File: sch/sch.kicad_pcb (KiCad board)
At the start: 2 copper layers, 53 parts, among them U1 Pico, U2 PCA9548ADB, U3 MPR121QR2_BOARD, U4 MPR121QR2_BOARD, U5 MPR121QR2_BOARD

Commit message: Updated schematic for Pro Micro
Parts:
- removed U1: Pico, MCU_RaspberryPi_and_Boards:RPi_Pico_SMD_TH
- added REF**: MountingHole_3.2mm_M3_DIN965_Pad, MountingHole:MountingHole_3.2mm_M3_DIN965_Pad, F.Cu at (269.1, 139.2)
- added REF**: MountingHole_3.2mm_M3_DIN965_Pad, MountingHole:MountingHole_3.2mm_M3_DIN965_Pad, F.Cu at (25.0, 45.0)
- added REF**: MountingHole_3.2mm_M3_DIN965_Pad, MountingHole:MountingHole_3.2mm_M3_DIN965_Pad, F.Cu at (269.1, 44.5)
- added REF**: MountingHole_3.2mm_M3_DIN965_Pad, MountingHole:MountingHole_3.2mm_M3_DIN965_Pad, F.Cu at (24.9, 139.2)
- added U6: ProMicro, promicro:ProMicro, F.Cu at (73.2, 58.4)
- moved KEY31 33.6 mm to (154.9, 89.2)
- moved KEY30 27.4 mm to (169.5, 116.0)
- moved R3 14.9 mm to (130.3, 133.1), turned to 180 degrees
- moved R4 14.6 mm to (130.3, 136.6), turned to 180 degrees
- moved KEY11 13.7 mm to (131.3, 48.8), turned to -90 degrees
- moved KEY9 13.1 mm to (191.6, 48.8), turned to -90 degrees
- moved TOF4 12.2 mm to (234.5, 139.6)
- moved TOF2 10.3 mm to (102.4, 139.6)
- moved R8 10.1 mm to (218.7, 133.1)
- moved R6 10.1 mm to (167.3, 132.9)
- moved R1 10.1 mm to (83.7, 133.4), turned to 180 degrees
- moved R2 10.0 mm to (83.7, 136.6), turned to 180 degrees
- moved U3 7.81 mm to (101.2, 68.5)
- moved U5 7.57 mm to (223.1, 68.5)
- moved KEY10 7.50 mm to (191.6, 63.4), turned to -90 degrees
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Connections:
- U2 pad 3: /MX_RST -> (no net)
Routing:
- net +3.3V: track 0.00 -> 517.3 mm, vias 0 -> 1
- net GND: track 0.00 -> 506.5 mm, vias 0 -> 1
- net /SDA: track 0.00 -> 387.2 mm, vias 0 -> 1
- net /SCL: track 0.00 -> 381.9 mm, vias 0 -> 1
- net /SDA4: track 0.00 -> 114.3 mm, vias 0 -> 2
- net /SCL4: track 0.00 -> 111.0 mm, vias 0 -> 2
- net /SCL1: track 0.00 -> 106.3 mm, vias 0 -> 4
- net /SDA1: track 0.00 -> 93.0 mm, vias 0 -> 2
- net Net-(KEY24-Pin_1): track 0.00 -> 91.6 mm, vias 0 -> 1
- net Net-(KEY11-Pin_1): track 0.00 -> 88.1 mm, vias 0 -> 1
- net Net-(KEY22-Pin_1): track 0.00 -> 83.4 mm, vias 0 -> 1
- net Net-(KEY12-Pin_1): track 0.00 -> 79.5 mm, vias 0 -> 1
- net Net-(KEY20-Pin_1): track 0.00 -> 73.6 mm, vias 0 -> 1
- net Net-(KEY26-Pin_1): track 0.00 -> 69.4 mm, vias 0 -> 1
- net Net-(KEY23-Pin_1): track 0.00 -> 68.3 mm
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- added copper zone on B.Cu, net GND
- added copper zone on F.Cu, net GND
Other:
- board outline added: 254.1 x 104.6 mm

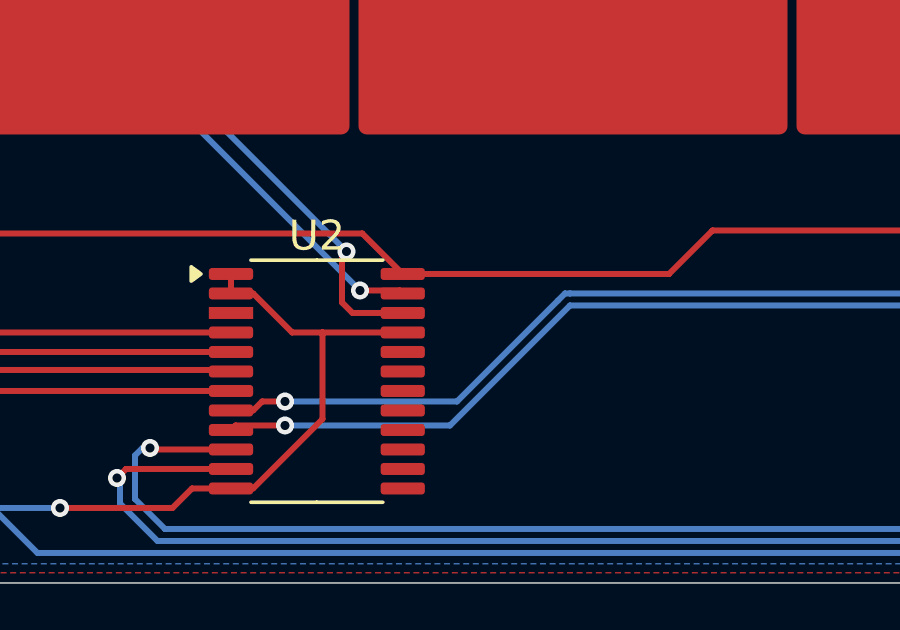
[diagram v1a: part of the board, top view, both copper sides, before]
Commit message: fixed missing pull up on multiplexer
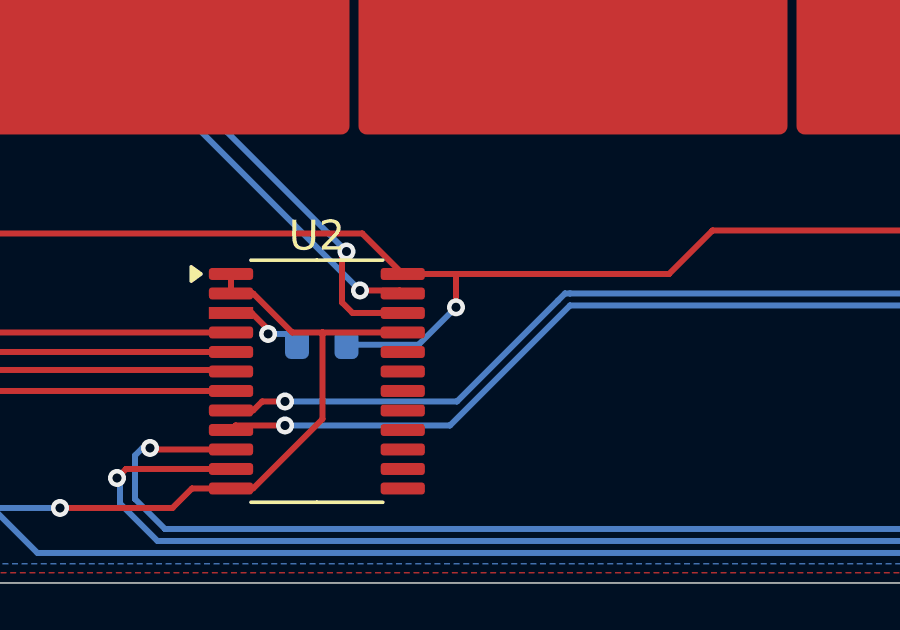
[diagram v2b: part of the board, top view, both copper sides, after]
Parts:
- added R9: 4.7K, Resistor_SMD:R_0603_1608Metric, B.Cu at (146.5, 136.7)
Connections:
- U2 pad 3: (no net) -> Net-(U2-~{RESET})
- U6 pad 18: (no net) -> unconnected-(U6-F6-Pad18)
- U6 pad 22: unconnected-(U6-RST-Pad22) -> GND
- U6 pad 23: GND -> unconnected-(U6-GND-Pad23)
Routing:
- net +3.3V: track 517.3 -> 522.5 mm, vias 1 -> 2
- net Net-(U2-~{RESET}): track 0.00 -> 2.74 mm, vias 0 -> 1

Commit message: Revision 2 of the PCB
Updated to using stm32f4 and a more modular design
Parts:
- removed KEY10, KEY11, KEY12, KEY13, KEY14, KEY15, KEY16, KEY17, KEY18, KEY19, KEY20, KEY21, KEY22, KEY23, KEY24, KEY25, KEY26, KEY27, KEY28, KEY29, KEY30, KEY31, KEY32, KEY33, KEY34, KEY35, KEY36, KEY9: Conn_01x01, chu_main:ChuKey
- removed REF** (x4): MountingHole_3.2mm_M3_DIN965_Pad, MountingHole:MountingHole_3.2mm_M3_DIN965_Pad
- removed TOF1, TOF2, TOF3, TOF4: Conn_01x06, Connector_PinSocket_2.54mm:PinSocket_1x06_P2.54mm_Vertical
- added C1: 10u, Capacitor_SMD:C_0603_1608Metric_Pad1.08x0.95mm_HandSolder, F.Cu at (157.6, 41.1)
- added C10: 100n, Capacitor_SMD:C_0603_1608Metric_Pad1.08x0.95mm_HandSolder, F.Cu at (170.5, 47.0)
- added C11: 100n, Capacitor_SMD:C_0603_1608Metric_Pad1.08x0.95mm_HandSolder, F.Cu at (158.3, 66.4)
- added C12: 33p, Capacitor_SMD:C_0603_1608Metric_Pad1.08x0.95mm_HandSolder, F.Cu at (171.0, 54.0)
- added C13: 33p, Capacitor_SMD:C_0603_1608Metric_Pad1.08x0.95mm_HandSolder, F.Cu at (171.0, 50.5)
- added C14: 22u, Capacitor_SMD:C_0805_2012Metric, F.Cu at (128.4, 50.5)
- added C15: 22u, Capacitor_SMD:C_0805_2012Metric, F.Cu at (133.4, 56.0)
- added C16: 100n, Capacitor_SMD:C_0603_1608Metric_Pad1.08x0.95mm_HandSolder, F.Cu at (131.6, 77.5)
- added C17: 100n, Capacitor_SMD:C_0603_1608Metric_Pad1.08x0.95mm_HandSolder, F.Cu at (144.1, 77.5)
- added C18: 100n, Capacitor_SMD:C_0603_1608Metric_Pad1.08x0.95mm_HandSolder, F.Cu at (160.5, 77.7)
- added C19: 100n, Capacitor_SMD:C_0603_1608Metric_Pad1.08x0.95mm_HandSolder, F.Cu at (172.9, 77.8)
- added C2: 100n, Capacitor_SMD:C_0603_1608Metric_Pad1.08x0.95mm_HandSolder, F.Cu at (168.1, 55.4)
- added C3: 100n, Capacitor_SMD:C_0603_1608Metric_Pad1.08x0.95mm_HandSolder, F.Cu at (164.3, 42.7)
- added C4: 100n, Capacitor_SMD:C_0603_1608Metric_Pad1.08x0.95mm_HandSolder, F.Cu at (157.6, 42.7)
- added C5: 100n, Capacitor_SMD:C_0603_1608Metric_Pad1.08x0.95mm_HandSolder, F.Cu at (152.9, 54.9)
- added C6: 100n, Capacitor_SMD:C_0603_1608Metric_Pad1.08x0.95mm_HandSolder, F.Cu at (165.1, 58.1)
- added C7: 10n, Capacitor_SMD:C_0603_1608Metric_Pad1.08x0.95mm_HandSolder, F.Cu at (168.2, 48.9)
- added C8: 1u, Capacitor_SMD:C_0603_1608Metric_Pad1.08x0.95mm_HandSolder, F.Cu at (171.1, 43.0)
- added C9: 1u, Capacitor_SMD:C_0603_1608Metric_Pad1.08x0.95mm_HandSolder, F.Cu at (171.1, 41.4)
- added D1: RED, LED_SMD:LED_0201_0603Metric, F.Cu at (123.2, 55.8)
- added D2: WS2812B, LED_SMD:LED_WS2812B_PLCC4_5.0x5.0mm_P3.2mm, F.Cu at (131.6, 81.2)
- added D3: WS2812B, LED_SMD:LED_WS2812B_PLCC4_5.0x5.0mm_P3.2mm, F.Cu at (144.0, 81.2)
- added D4: WS2812B, LED_SMD:LED_WS2812B_PLCC4_5.0x5.0mm_P3.2mm, F.Cu at (160.5, 81.3)
- added D5: WS2812B, LED_SMD:LED_WS2812B_PLCC4_5.0x5.0mm_P3.2mm, F.Cu at (172.9, 81.4)
- added FB1: 120R, Inductor_SMD:L_0603_1608Metric, F.Cu at (168.4, 42.2)
- added J1: USB_C_Receptacle_USB2.0_16P, Connector_USB:USB_C_Receptacle_GCT_USB4105-xx-A_16P_TopMnt_Horizontal, F.Cu at (134.5, 43.1)
- added J2: Conn_01x04_Pin, Connector_PinHeader_2.54mm:PinHeader_1x04_P2.54mm_Vertical, F.Cu at (150.2, 41.5)
- added J3: Conn_01x04, chu_main:Conn_Solder_I2C, F.Cu at (181.4, 72.5)
- added J4: Conn_01x06_Socket, Connector_PinHeader_2.54mm:PinHeader_1x06_P2.54mm_Vertical, F.Cu at (146.2, 146.0)
- added J5: Conn_01x04, chu_main:Conn_Solder_I2C, F.Cu at (123.0, 72.5)
- added J6: Conn_01x01, chu_main:Solder_3P, F.Cu at (121.9, 80.5)
- added J7: Conn_01x01, chu_main:Solder_3P, F.Cu at (182.5, 80.5)
- added MH1: M3, MountingHole:MountingHole_3.2mm_M3_Pad_Via, F.Cu at (122.5, 43.5)
- added MH2: M3, MountingHole:MountingHole_3.2mm_M3_Pad_Via, F.Cu at (181.5, 43.5)
- added MH3: M3, MountingHole:MountingHole_3.2mm_M3_Pad_Via, F.Cu at (122.5, 145.5)
- added MH4: M3, MountingHole:MountingHole_3.2mm_M3_Pad_Via, F.Cu at (181.5, 145.5)
- added R10: 2k2, Resistor_SMD:R_0603_1608Metric_Pad0.98x0.95mm_HandSolder, F.Cu at (140.0, 56.0)
- added R11: 0, Resistor_SMD:R_0603_1608Metric_Pad0.98x0.95mm_HandSolder, F.Cu at (144.0, 68.2)
- added R12: 0, Resistor_SMD:R_0603_1608Metric_Pad0.98x0.95mm_HandSolder, F.Cu at (147.0, 68.2)
- added R13: 2k2, Resistor_SMD:R_0603_1608Metric_Pad0.98x0.95mm_HandSolder, F.Cu at (163.2, 59.9)
- added R14: 2k2, Resistor_SMD:R_0603_1608Metric_Pad0.98x0.95mm_HandSolder, F.Cu at (159.9, 59.9)
- added R15: 0, Resistor_SMD:R_0603_1608Metric_Pad0.98x0.95mm_HandSolder, F.Cu at (150.0, 68.2)
- added R16: 2k2, Resistor_SMD:R_0603_1608Metric_Pad0.98x0.95mm_HandSolder, F.Cu at (140.6, 65.3)
- added R17: 0, Resistor_SMD:R_0603_1608Metric_Pad0.98x0.95mm_HandSolder, F.Cu at (153.0, 68.2)
- added R18: 0, Resistor_SMD:R_0603_1608Metric_Pad0.98x0.95mm_HandSolder, F.Cu at (142.5, 68.2)
- added R19: 0, Resistor_SMD:R_0603_1608Metric_Pad0.98x0.95mm_HandSolder, F.Cu at (145.5, 68.2)
- added R20: 0, Resistor_SMD:R_0603_1608Metric_Pad0.98x0.95mm_HandSolder, F.Cu at (148.5, 68.2)
- added R21: 0, Resistor_SMD:R_0603_1608Metric_Pad0.98x0.95mm_HandSolder, F.Cu at (151.5, 68.2)
- added R22: 2k2, Resistor_SMD:R_0603_1608Metric_Pad0.98x0.95mm_HandSolder, F.Cu at (140.8, 145.2)
- added R23: 2k2, Resistor_SMD:R_0603_1608Metric_Pad0.98x0.95mm_HandSolder, F.Cu at (140.8, 146.8)
- added R24: 1k, Resistor_SMD:R_0603_1608Metric_Pad0.98x0.95mm_HandSolder, F.Cu at (123.2, 58.7)
- added RST: SW_SPST, Button_Switch_SMD:SW_SPST_TS-1088-xR025, F.Cu at (172.0, 61.1)
- added U1: MPR121QR2, Package_DFN_QFN:UQFN-20_3x3mm_P0.4mm, F.Cu at (162.0, 68.5)
- added Y1: 25MHz, Crystal:Crystal_SMD_3225-4Pin_3.2x2.5mm_HandSoldering, F.Cu at (174.2, 52.1)
- R1, R2, R3, R4: value 4.7K -> 0; footprint Resistor_SMD:R_0603_1608Metric -> Resistor_SMD:R_0603_1608Metric_Pad0.98x0.95mm_HandSolder
- R5: value 4.7K -> 10K; footprint Resistor_SMD:R_0603_1608Metric -> Resistor_SMD:R_0603_1608Metric_Pad0.98x0.95mm_HandSolder
- R6, R8: value 4.7K -> 5.1K; footprint Resistor_SMD:R_0603_1608Metric -> Resistor_SMD:R_0603_1608Metric_Pad0.98x0.95mm_HandSolder
- R7: value 4.7K -> 75K; footprint Resistor_SMD:R_0603_1608Metric -> Resistor_SMD:R_0603_1608Metric_Pad0.98x0.95mm_HandSolder
- R9: value 4.7K -> 2k2; footprint Resistor_SMD:R_0603_1608Metric -> Resistor_SMD:R_0603_1608Metric_Pad0.98x0.95mm_HandSolder; moved to F.Cu
- U2: value PCA9548ADB -> STM32F411R_C-E_Tx; footprint Package_SO:TSSOP-24_4.4x7.8mm_P0.65mm -> Package_QFP:LQFP-64_10x10mm_P0.5mm
- U3: value MPR121QR2_BOARD -> PCA9548ADB; footprint chu_main:MPR121_BOARD -> Package_SO:TSSOP-24_4.4x7.8mm_P0.65mm; moved to F.Cu
- U4: value MPR121QR2_BOARD -> AMS1117-3.3; footprint chu_main:MPR121_BOARD -> Package_TO_SOT_SMD:SOT-223-3_TabPin2; moved to F.Cu
- U5: value MPR121QR2_BOARD -> SN74LV1T34DBV; footprint chu_main:MPR121_BOARD -> Package_TO_SOT_SMD:SOT-23-5; moved to F.Cu
- U6: value ProMicro -> USBLC6-2SC6; footprint promicro:ProMicro -> Package_TO_SOT_SMD:SOT-23-6
- moved KEY2 129.9 mm to (127.7, 126.1), turned to 0 degrees
- moved KEY1 129.8 mm to (127.7, 98.1), turned to 0 degrees
- moved R8 125.7 mm to (128.0, 46.1), turned to 90 degrees
- moved R2 103.9 mm to (157.6, 63.6), turned to 90 degrees
- moved R1 100.6 mm to (156.1, 63.6), turned to 90 degrees
- moved KEY4 99.1 mm to (144.0, 126.1), turned to 0 degrees
- moved KEY3 99.0 mm to (144.0, 98.0), turned to 0 degrees
- moved R7 91.4 mm to (157.4, 68.9), turned to 90 degrees
- moved R6 90.7 mm to (141.0, 46.1), turned to 90 degrees
- moved U2 88.7 mm to (160.5, 50.3), turned to 180 degrees
- moved U5 87.5 mm to (135.8, 62.2), turned to 90 degrees
- moved R9 81.1 mm to (138.5, 56.0), turned to 90 degrees
- moved R4 79.5 mm to (160.1, 62.9), turned to 0 degrees
- moved R3 74.8 mm to (160.0, 64.5), turned to 0 degrees
- moved U6 73.9 mm to (146.9, 52.3), turned to 0 degrees
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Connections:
- R1 pad 1: +3.3V -> /MPR121_ADDR
- R1 pad 2: /SCL1 -> GND
- R2 pad 1: +3.3V -> /MPR121_ADDR
- R2 pad 2: /SDA1 -> +3.3V
- R3 pad 1: +3.3V -> /MPR121_ADDR
- R3 pad 2: /SCL2 -> /I2C1_SDA
- R4 pad 1: +3.3V -> /MPR121_ADDR
- R4 pad 2: /SDA2 -> /I2C1_SCL
- R5 pad 1: +3.3V -> Net-(SW1-A)
- R5 pad 2: /SCL3 -> /BOOT0
- R6 pad 1: +3.3V -> GND
- R6 pad 2: /SDA3 -> /USB_CC1
- R7 pad 1: +3.3V -> Net-(U1-REXT)
- R7 pad 2: /SCL4 -> GND
- R8 pad 1: +3.3V -> GND
- R8 pad 2: /SDA4 -> /USB_CC2
- R9 pad 2: Net-(U2-~{RESET}) -> /I2C3_SDA
- U2 pad 1: GND -> +3.3V
- U2 pad 10: /SDA4 -> unconnected-(U2-PC2-Pad10)
- U2 pad 11: /SCL4 -> unconnected-(U2-PC3-Pad11)
- U2 pad 13: unconnected-(U2-SD4-Pad13) -> +3.3VA
- U2 pad 18: unconnected-(U2-SC6-Pad18) -> GND
- U2 pad 19: unconnected-(U2-SD7-Pad19) -> +3.3V
- U2 pad 2: GND -> unconnected-(U2-PC13-Pad2)
- U2 pad 21: GND -> unconnected-(U2-PA5-Pad21)
- U2 pad 22: /SCL -> unconnected-(U2-PA6-Pad22)
- U2 pad 23: /SDA -> unconnected-(U2-PA7-Pad23)
- U2 pad 24: +3.3V -> unconnected-(U2-PC4-Pad24)
- U2 pad 3: Net-(U2-~{RESET}) -> unconnected-(U2-PC14-Pad3)
- U2 pad 4: /SDA1 -> unconnected-(U2-PC15-Pad4)
- U2 pad 5: /SCL1 -> /HSE_IN
- U2 pad 6: /SDA2 -> /HSE_OUT
- U2 pad 7: /SCL2 -> /NRST
- U2 pad 8: /SDA3 -> unconnected-(U2-PC0-Pad8)
- U2 pad 9: /SCL3 -> unconnected-(U2-PC1-Pad9)
- U3 pad 1: unconnected-(U3-~{IRQ}-Pad1) -> GND
- U3 pad 10: Net-(KEY15-Pin_1) -> /SDA4
- U3 pad 11: Net-(KEY16-Pin_1) -> /SCL4
- U3 pad 12: Net-(KEY17-Pin_1) -> GND
- U3 pad 13: Net-(KEY18-Pin_1) -> unconnected-(U3-SD4-Pad13)
- U3 pad 14: Net-(KEY19-Pin_1) -> unconnected-(U3-SC4-Pad14)
- U3 pad 15: Net-(KEY20-Pin_1) -> unconnected-(U3-SD5-Pad15)
- U3 pad 16: Net-(KEY21-Pin_1) -> unconnected-(U3-SC5-Pad16)
- U3 pad 17: Net-(KEY22-Pin_1) -> unconnected-(U3-SD6-Pad17)
- U3 pad 18: Net-(KEY23-Pin_1) -> unconnected-(U3-SC6-Pad18)
- U3 pad 19: Net-(KEY24-Pin_1) -> unconnected-(U3-SD7-Pad19)
- U3 pad 2: /SCL -> GND
- U3 pad 20: +3.3V -> unconnected-(U3-SC7-Pad20)
- U3 pad 3: /SDA -> Net-(U3-~{RESET})
- U3 pad 4: +3.3V -> /SDA1
- U3 pad 6: GND -> /SDA2
- U3 pad 8: Net-(KEY13-Pin_1) -> /SDA3
- U3 pad 9: Net-(KEY14-Pin_1) -> /SCL3
- U4 pad 1: unconnected-(U4-~{IRQ}-Pad1) -> GND
- U4 pad 2: /SCL -> +3.3V
- U4 pad 3: /SDA -> VBUS
- U5 pad 2: /SCL -> Net-(D2-DIN)
- U5 pad 3: /SDA -> GND
- U5 pad 4: GND -> /LED_DIN
- U6 pad 1: unconnected-(U6-TX-Pad1) -> /USB_D-
- U6 pad 2: unconnected-(U6-RX-Pad2) -> GND
- U6 pad 3: GND -> /USB_D+
- U6 pad 4: GND -> /USB_D+
- U6 pad 5: /SDA -> VBUS
- U6 pad 6: /SCL -> /USB_D-
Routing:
- net GND: track 506.5 -> 14.8 mm, vias 1 -> 54
- net /SDA: track 387.2 -> 0.00 mm, vias 1 -> 0
- net /SCL: track 381.9 -> 0.00 mm, vias 1 -> 0
- net +3.3V: track 522.5 -> 280.2 mm, vias 2 -> 14
- net /SDA_ToF: track 0.00 -> 187.6 mm, vias 0 -> 2
- net /SCL_ToF: track 0.00 -> 184.7 mm, vias 0 -> 2
- net VBUS: track 0.00 -> 125.2 mm, vias 0 -> 6
- net /SDA4: track 114.3 -> 4.63 mm, vias 2 -> 0
- net /SCL4: track 111.0 -> 5.57 mm, vias 2 -> 0
- net /SCL1: track 106.3 -> 4.74 mm, vias 4 -> 0
- net Net-(KEY24-Pin_1): track 91.6 -> 0.00 mm, vias 1 -> 0
- net Net-(KEY11-Pin_1): track 88.1 -> 0.00 mm, vias 1 -> 0
- net /SDA1: track 93.0 -> 5.53 mm, vias 2 -> 0
- net /I2C1_SCL: track 0.00 -> 84.5 mm, vias 0 -> 4
- net Net-(KEY22-Pin_1): track 83.4 -> 0.00 mm, vias 1 -> 0
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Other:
- board size 254.1 x 104.6 mm -> 67 x 110 mm
- rule pad_to_mask_clearance: 0 -> 0.1

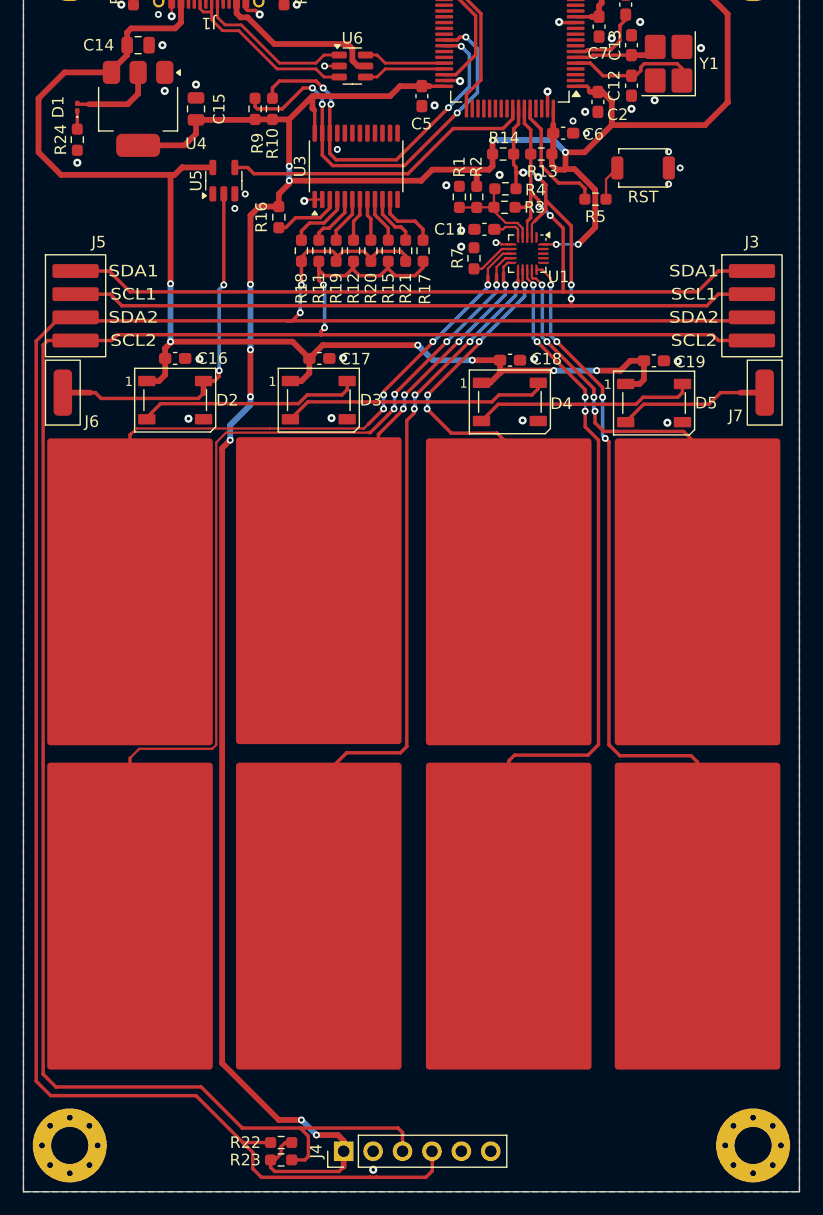
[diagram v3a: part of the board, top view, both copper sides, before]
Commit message: Updated side pads with power and ground
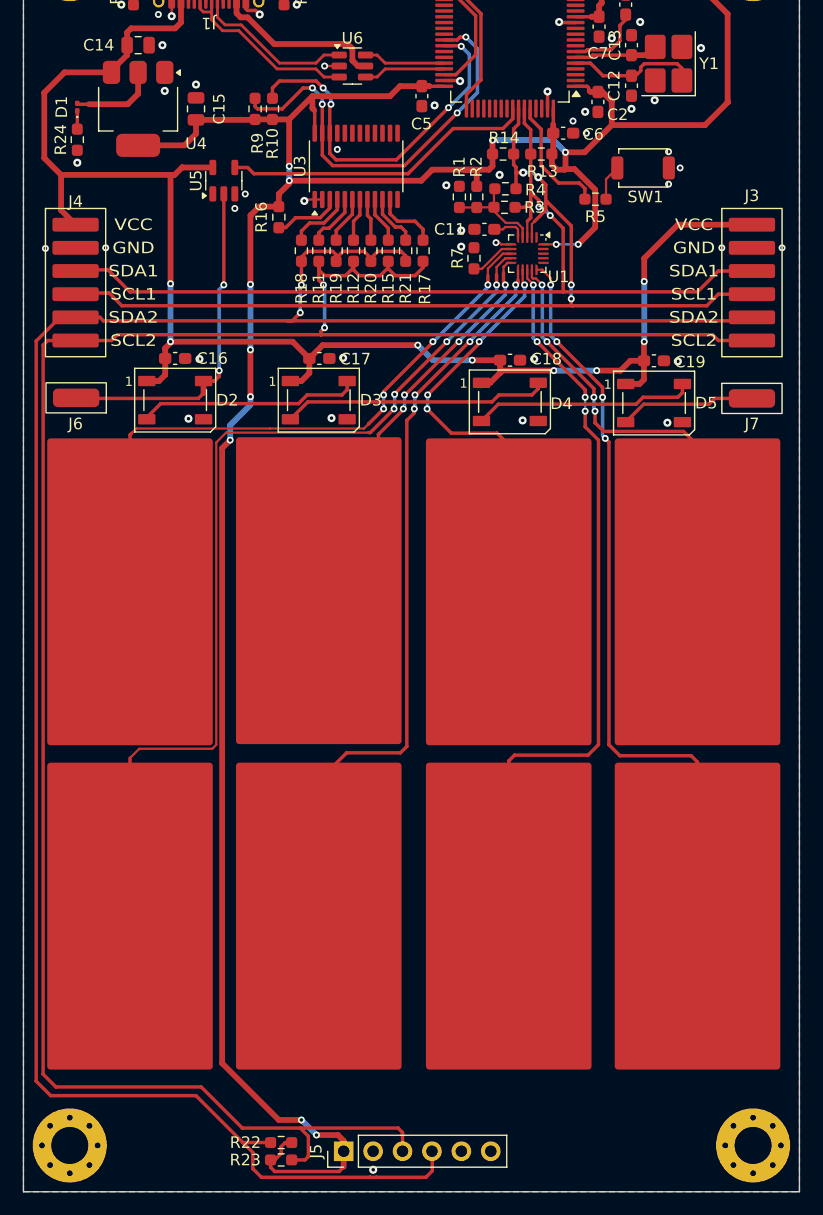
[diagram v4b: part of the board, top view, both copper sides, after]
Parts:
- J3: value Conn_01x04 -> Conn_01x06
- J4: renamed from J5; value Conn_01x04 -> Conn_01x06
- moved J4 1.50 mm to (123.0, 71.0)
- moved J6 1.23 mm to (123.0, 81.0), turned to 180 degrees
- moved J7 1.21 mm to (181.4, 81.0), turned to 0 degrees
- renumbered J4 to J5, RST to SW1
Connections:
- J3 pad 1: /I2C1_SDA -> VBUS
- J3 pad 2: /I2C1_SCL -> GND
- J3 pad 3: /SDA_ToF -> /I2C1_SDA
- J3 pad 4: /SCL_ToF -> /I2C1_SCL
- J4 pad 1: /I2C1_SDA -> VBUS
- J4 pad 2: /I2C1_SCL -> GND
- J4 pad 3: /SDA_ToF -> /I2C1_SDA
- J4 pad 4: /SCL_ToF -> /I2C1_SCL
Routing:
- net VBUS: track 125.2 -> 148.9 mm, vias 6 -> 8
- net Net-(D2-DIN): track 30.9 -> 29.6 mm
- net Net-(D5-DOUT): track 13.1 -> 11.7 mm
- net GND: vias 54 -> 58

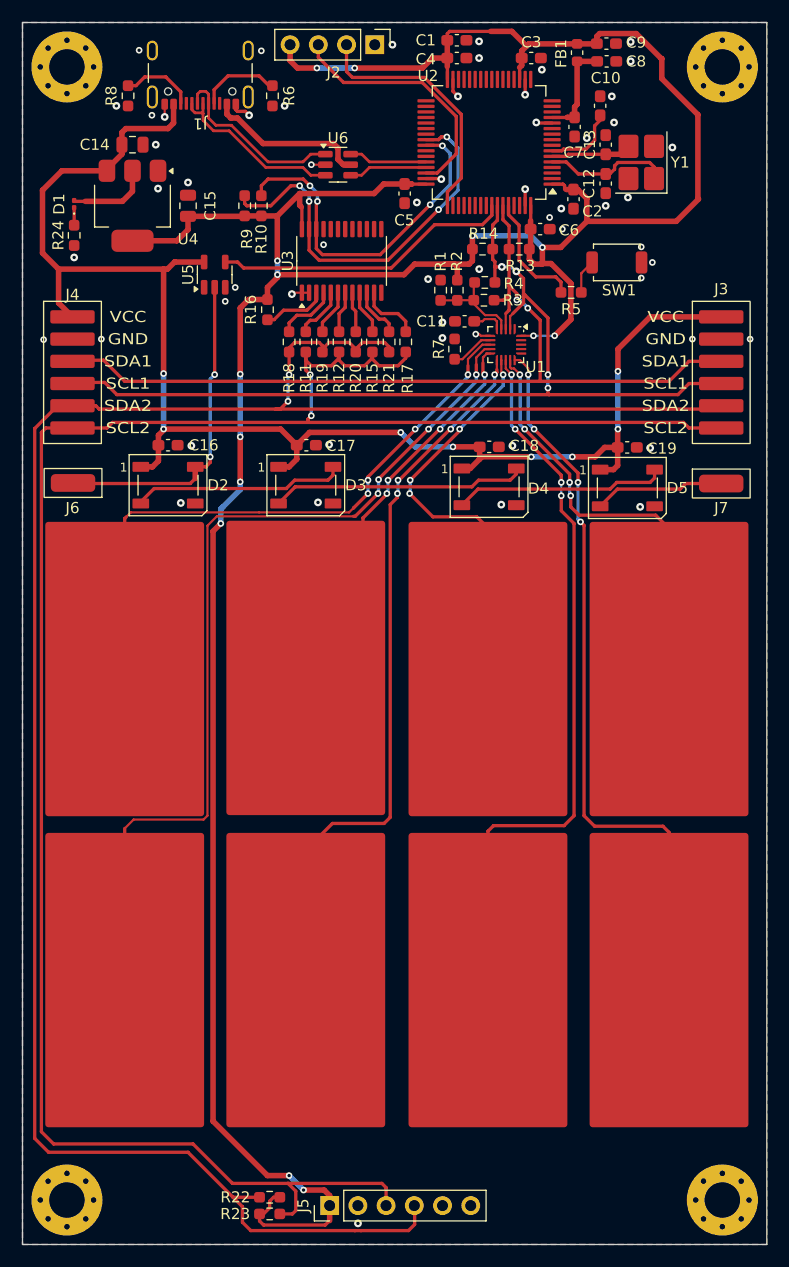
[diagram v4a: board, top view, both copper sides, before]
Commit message: gpy2 sensor instead of tof
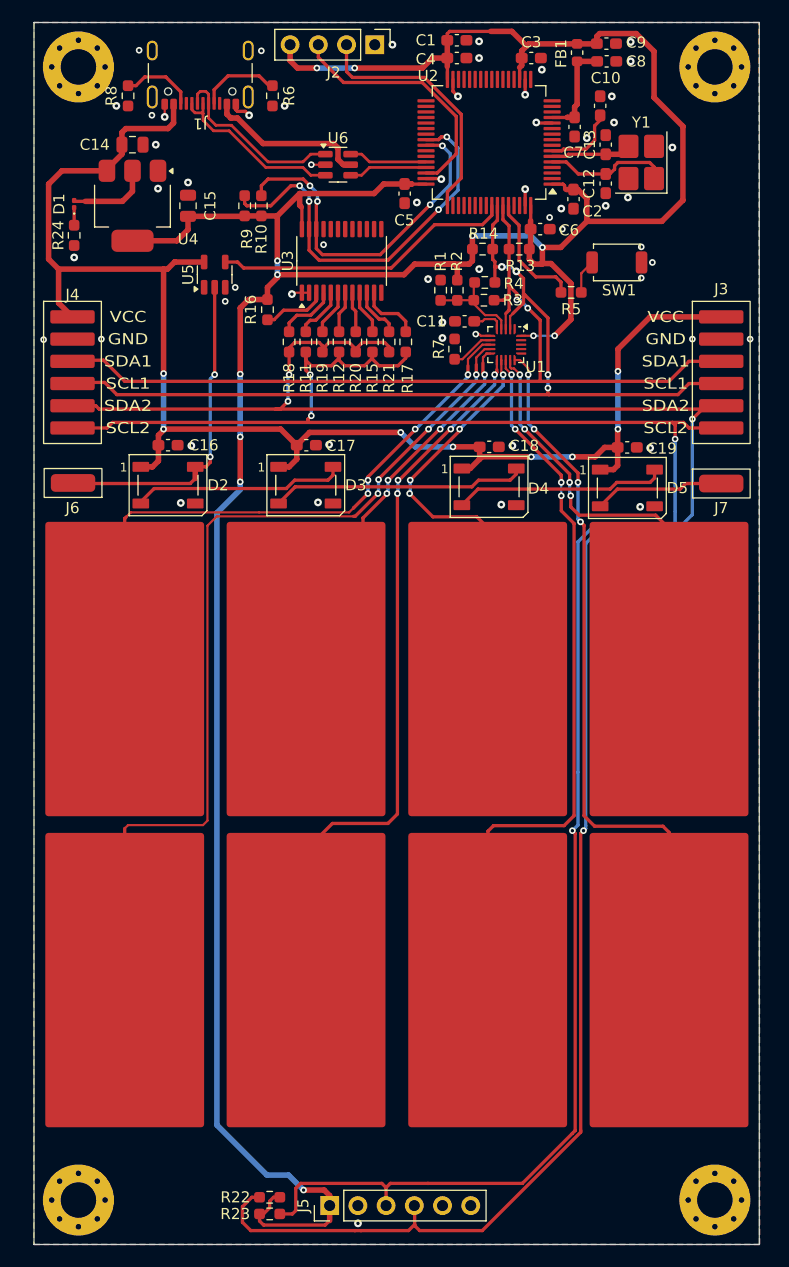
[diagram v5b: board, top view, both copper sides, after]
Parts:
- moved MH1 1.03 mm to (123.5, 43.5)
- moved MH3 1.03 mm to (123.5, 145.5)
- moved MH2 0.68 mm to (180.8, 43.5)
- moved MH4 0.68 mm to (180.8, 145.5)
- moved KEY3 0.10 mm to (144.0, 98.1)
- moved KEY4 0.05 mm to (144.1, 126.1)
- moved KEY6 0.05 mm to (160.3, 126.1)
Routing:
- net /SDA_ToF: track 188.0 -> 193.9 mm, vias 2 -> 4
- net +3.3V: track 280.2 -> 278.0 mm, vias 14 -> 12
- net /SCL_ToF: track 185.0 -> 184.7 mm, vias 2 -> 4
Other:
- board size 67 x 110 mm -> 65.3 x 110 mm
